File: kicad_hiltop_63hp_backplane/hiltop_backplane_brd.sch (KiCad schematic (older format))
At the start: 20 parts

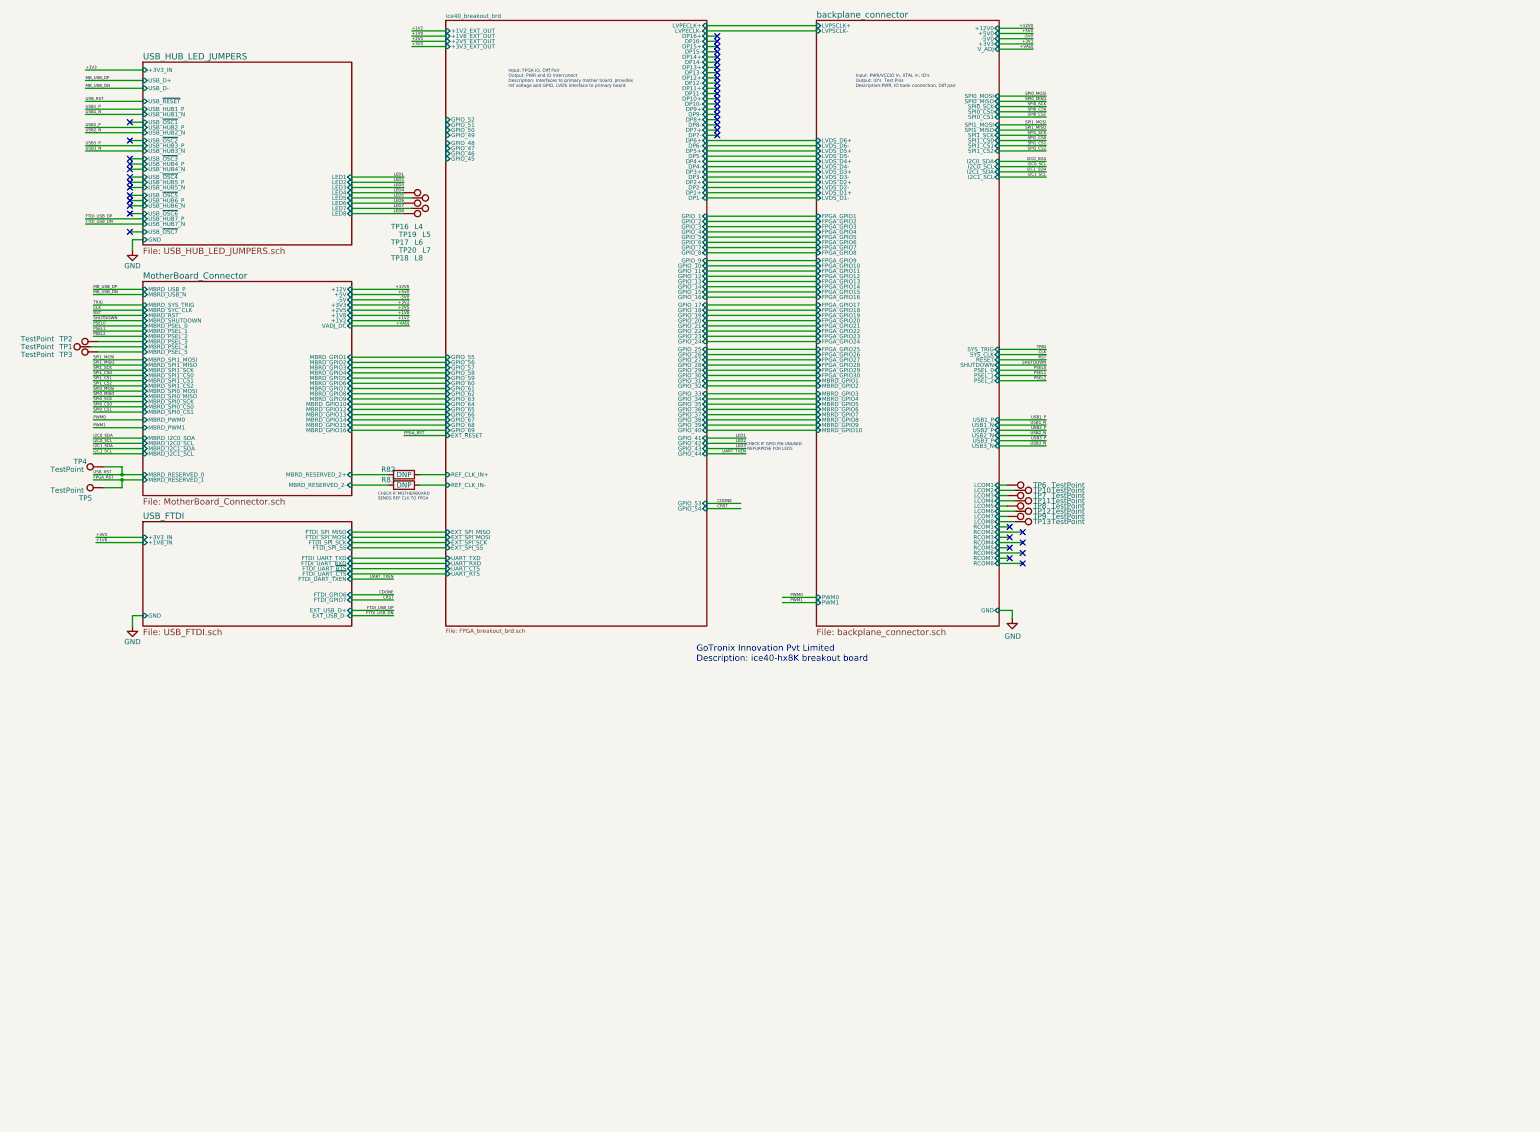
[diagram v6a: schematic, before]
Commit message: updated FPGA/SOC module pinouts
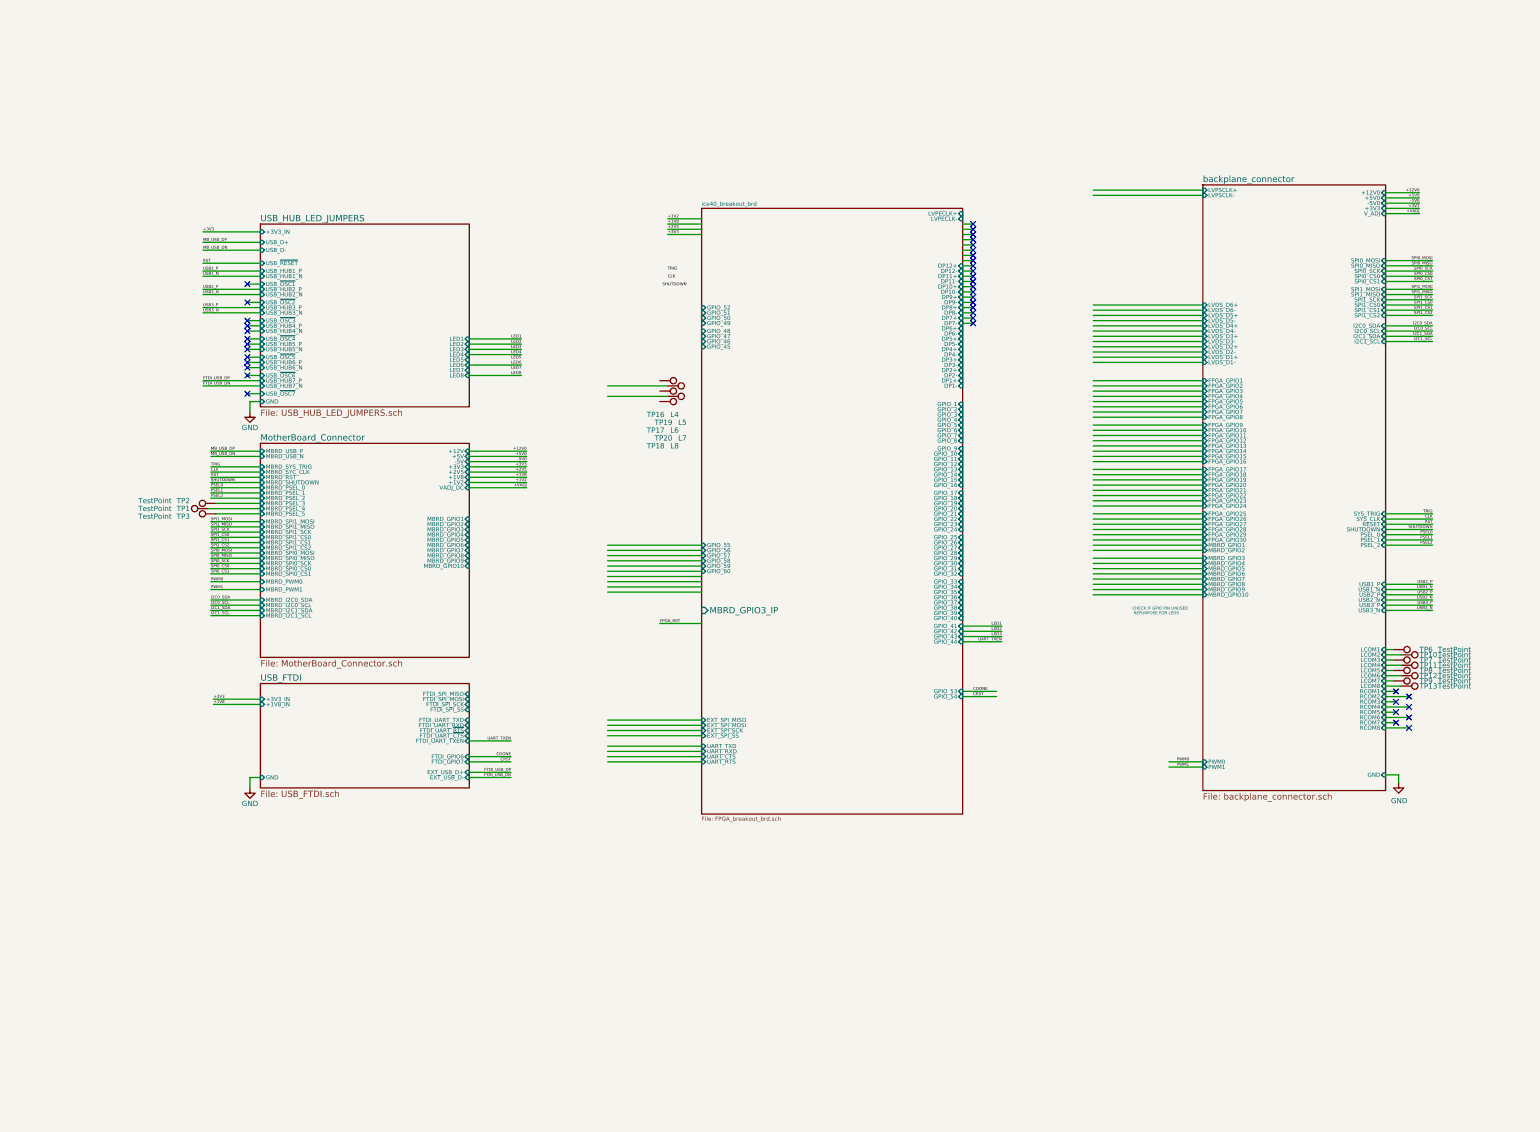
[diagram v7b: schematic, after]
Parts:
- removed R82, R83: DNP, Resistor_SMD:R_0402_1005Metric, symbol hiltop_backplane_brd-rescue:R-device-hiltop_backplane_brd-rescue
- removed TP4, TP5: TestPoint, TestPoint:TestPoint_Pad_D1.0mm, symbol hiltop_backplane_brd-rescue:TestPoint-Connector-hiltop_backplane_brd-rescue
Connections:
- net labels removed: USB_RST
- wire segments 254 -> 237
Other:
- note removed: "CHECK IF MOTHERBOARD \nSENDS REF CLK TO FPGA"
- note removed: "GoTronix Innovation Pvt Limited\nDescription: ice40-hx8K breakout board"
- note removed: "Input: FPGA IO, Diff Pair \nOutput: PWR and IO interconect \nDescription: Interfaces to primary mother board, provides \nref voltage and GPIO, LVDS interface to primary board"
- note removed: "Input: PWR/VCCIO in, XTAL in, IO's\nOutput: IO's Test Pins\nDescription:PWR, IO bank connection, Diff pair"
- moved on the sheet: TP1, TP10, TP11, TP12, TP13, TP16, TP17, TP18, TP19, TP2, TP20, TP3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

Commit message: updated schematics to RevC including general tidy up
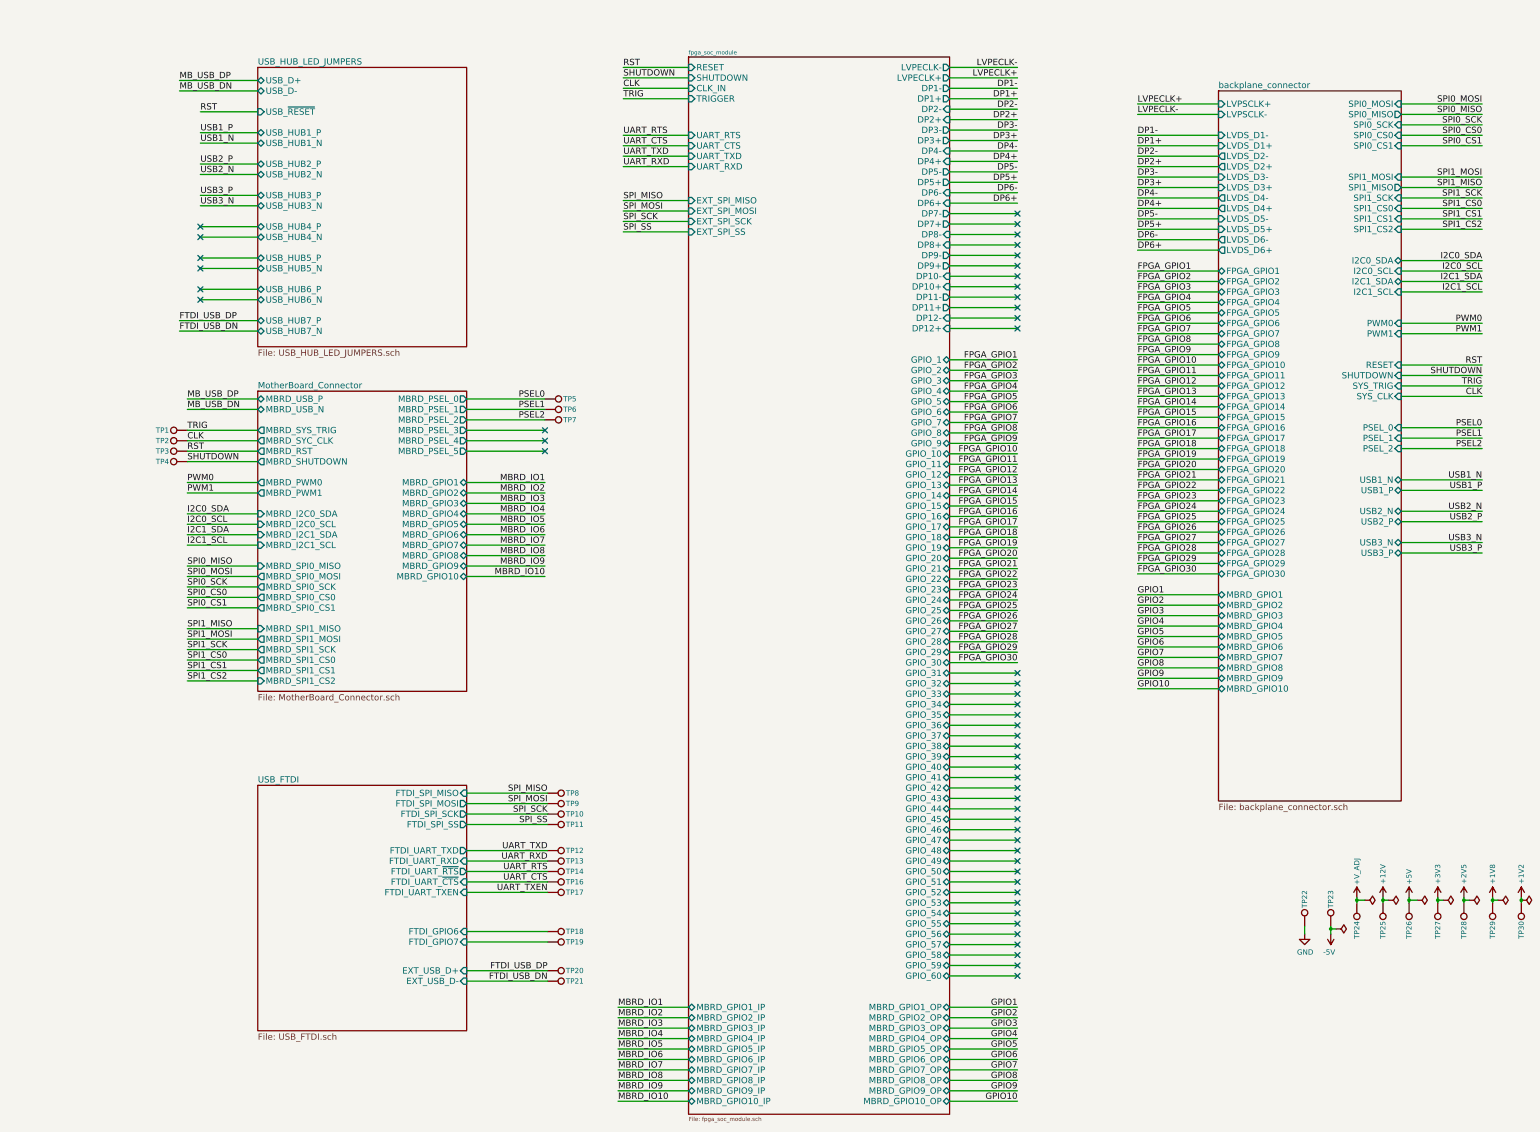
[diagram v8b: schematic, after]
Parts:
- added TP14, TP21, TP22, TP23, TP24, TP25, TP26, TP27, TP28, TP29, TP30, TP4, TP5: TestPoint, TestPoint:TestPoint_Pad_D1.0mm, symbol hiltop_backplane_brd-rescue:TestPoint-Connector-hiltop_backplane_brd-rescue
- TP16: value L4 -> TestPoint
- TP17: value L6 -> TestPoint
- TP18: value L8 -> TestPoint
- TP19: value L5 -> TestPoint
- TP20: value L7 -> TestPoint
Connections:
- net labels added: +12V, +5V, +V_ADJ, -5V, DP1+, DP1-, DP2+, DP2-, DP3+, DP3-, DP4+, DP4-, DP5+, DP5-, DP6+, DP6-, FPGA_GPIO1, FPGA_GPIO10, FPGA_GPIO11, FPGA_GPIO12, FPGA_GPIO13, FPGA_GPIO14, FPGA_GPIO15, FPGA_GPIO16, FPGA_GPIO17, FPGA_GPIO18, FPGA_GPIO19, FPGA_GPIO2, FPGA_GPIO20, FPGA_GPIO21, FPGA_GPIO22, FPGA_GPIO23, FPGA_GPIO24, FPGA_GPIO25, FPGA_GPIO26, FPGA_GPIO27, FPGA_GPIO28, FPGA_GPIO29, FPGA_GPIO3, FPGA_GPIO30, FPGA_GPIO4, FPGA_GPIO5, FPGA_GPIO6, FPGA_GPIO7, FPGA_GPIO8, FPGA_GPIO9, GPIO1, GPIO10, GPIO2, GPIO3, GPIO4, GPIO5, GPIO6, GPIO7, GPIO8, GPIO9, LVPECLK+, LVPECLK-, MBRD_IO1, MBRD_IO10, MBRD_IO2, MBRD_IO3, MBRD_IO4, MBRD_IO5, MBRD_IO6, MBRD_IO7, MBRD_IO8, MBRD_IO9, SPI_MISO, SPI_MOSI, SPI_SCK, SPI_SS, UART_CTS, UART_RTS, UART_RXD, UART_TXD
- net labels removed: +12V0, +5V0, +VADJ, -5V0, CDONE, CRST, FPGA_RST, LED1, LED2, LED3, LED4, LED5, LED6, LED7, LED8
- wire segments 237 -> 295
- no-connect marks 41 -> 51
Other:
- note removed: "CHECK IF GPIO PIN UNUSED\n REPURPOSE FOR LEDS"
